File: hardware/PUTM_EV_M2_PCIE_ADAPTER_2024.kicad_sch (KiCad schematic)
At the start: 2 parts, among them J1 PCIE-064-02-X-D-RA, J2 M_2_EdgeConector

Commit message: high speed signals routing done
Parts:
- added C1, C3, C5: 100nF, Capacitor_SMD:C_0402_1005Metric, symbol Device:C_Small
- added C2, C4, C6, C7, C8, C9: 1uF, Capacitor_SMD:C_0603_1608Metric, symbol Device:C_Small
- added J3: PCB_WIRE, Connector_Wire:SolderWire-0.1sqmm_1x04_P3.6mm_D0.4mm_OD1mm_Relief, symbol Connector:Conn_01x04_Pin
- added R1: 0, Resistor_SMD:R_0402_1005Metric, symbol Device:R_Small
- J2: value M_2_EdgeConector -> M2_KEY_M; footprint M2-PCIe-adapter-footprints:M_2_EdgeConnector -> Snapeda:M.2-KEY-M
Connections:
- net GND: now reaches J2.1 (GND)
- net GND: now also J1.A04 (GND), J1.A12 (GND), J1.A15 (GND), J1.A18 (GND), J1.A20 (GND), J1.A23 (GND), J1.A24 (GND), J1.A27 (GND), J1.A28 (GND), J1.A31 (GND), J1.B04 (GND), J1.B07 (GND), J1.B13 (GND), J1.B16 (GND), J1.B18 (GND), J1.B21 (GND), J1.B22 (GND), J1.B25 (GND), J1.B26 (GND), J1.B29 (GND), J1.B32 (GND), J2.15 (GND), J2.21 (GND), J2.27 (GND), J2.3 (GND), J2.33 (GND), J2.39 (GND), J2.45 (GND), J2.51 (GND), J2.52 (CLKREQ#), J2.57 (GND), J2.71 (GND), J2.73 (GND), J2.75 (GND), J2.9 (GND), J2.MH, C1.2, C2.2, C3.2, C4.2, C5.2, C6.2, C7.2, C8.2, C9.2, J3.2 (Pin_2), J3.3 (Pin_3)
- net DO3-: now reaches J2.11 (PET3-)
- net DO3-: now also J1.B28 (DO3-)
- net +3.3V: now reaches J2.12 (+3.3V)
- net +3.3V: now also J1.A09 (+3.3V), J1.A10 (+3.3V), J1.B08 (+3.3V), J2.14 (+3.3V), J2.16 (+3.3V), J2.18 (+3.3V), J2.2 (+3.3V), J2.4 (+3.3V), J2.70 (+3.3V), J2.72 (+3.3V), J2.74 (+3.3V), C3.1, C4.1, C7.1, C8.1, C9.1, R1.1
- net DO3+: now reaches J2.13 (PET3+)
- net DO3+: now also J1.B27 (DO3+)
- net DI2-: now reaches J2.17 (PER2-)
- net DI2-: now also J1.A26 (DI2-)
- net DI2+: now reaches J2.19 (PER2+)
- net DI2+: now also J1.A25 (DI2+)
- net DO2-: now reaches J2.23 (PET2-)
- net DO2-: now also J1.B24 (DO2-)
- net DO2+: now reaches J2.25 (PET2+)
- net DO2+: now also J1.B23 (DO2+)
- net DI1-: now reaches J2.29 (PER1-)
- net DI1-: now also J1.A22 (DI1+)
- net DI1+: now reaches J2.31 (PER1+)
- net DI1+: now also J1.A21 (DI1+)
- net DO1-: now reaches J2.35 (PET1-)
- net DO1-: now also J1.B20 (DO1-)
- net DO1+: now reaches J2.37 (PET1+)
- net DO1+: now also J1.B19 (DO1+)
- net DI0-: now reaches J2.41 (SATA-B+/PER0-)
- net DI0-: now also J1.A17 (DI0-)
- net DI0+: now reaches J2.43 (SATA-B-/PER0+)
- net DI0+: now also J1.A16 (DI0+)
- net DO0-: now reaches J2.47 (SATA-A-/PET0-)
- net DO0-: now also J1.B15 (DO0-)
- net DO0+: now reaches J2.49 (SATA-A+/PET0+)
- net DO0+: now also J1.B14 (DO0+)
- net DI3-: now reaches J2.5 (PER3-)
- net DI3-: now also J1.A30 (DI3-)
- net PWRGD: now reaches J2.50 (PERST#)
- net PWRGD: now also J1.A11 (PWRGD)
- net REFCLK-: now reaches J2.53 (REFCLK-)
- net REFCLK-: now also J1.A14 (REFCLK-)
- net WAKE#: now reaches J2.54 (PEWAKE#)
- net WAKE#: now also J1.B11 (WAKE#)
- net REFCLK+: now reaches J2.55 (REFCLK+)
- net REFCLK+: now also J1.A13 (REFCLK+)
- net DI3+: now reaches J2.7 (PER3+)
- net DI3+: now also J1.A29 (DI3+)
- net +3.3AUX: now reaches J1.B10 (+3.3VAUX)
- net +3.3AUX: now also C5.1, C6.1, R1.2
- new net +12V: C1.1, C2.1, J1.A02 (+12V), J1.A03 (+12V), J1.B01 (+12V), J1.B02 (+12V), J1.B03 (+12V), J3.1 (Pin_1)
- new net +5V: J3.4 (Pin_4)
- no-connect marks 0 -> 17
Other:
- moved on the sheet: J1

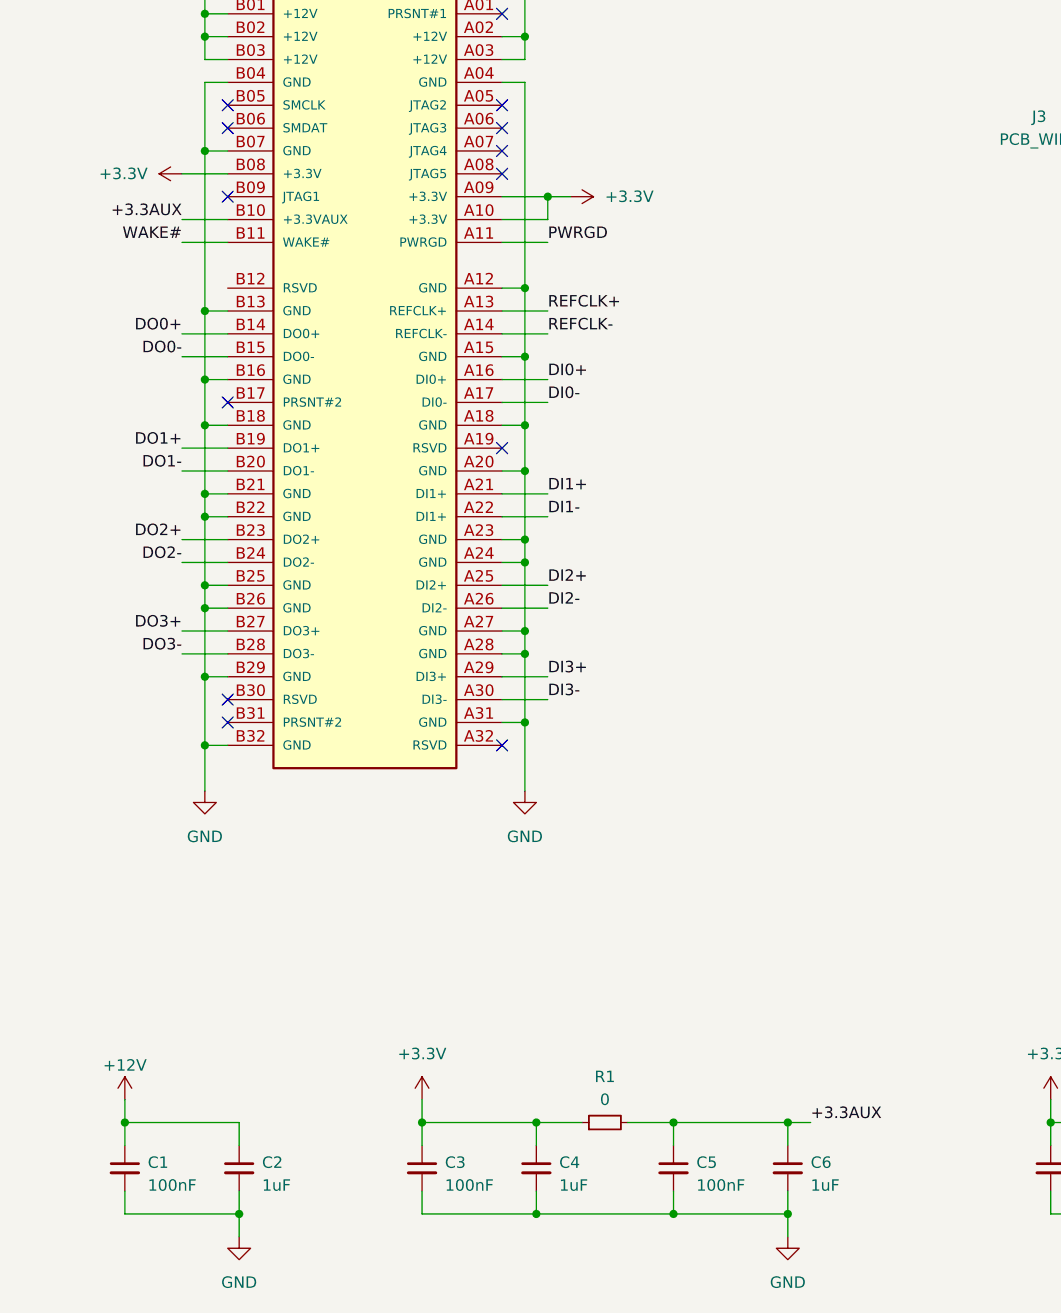
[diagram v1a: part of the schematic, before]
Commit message: deleted all tracks, needs a bigger board
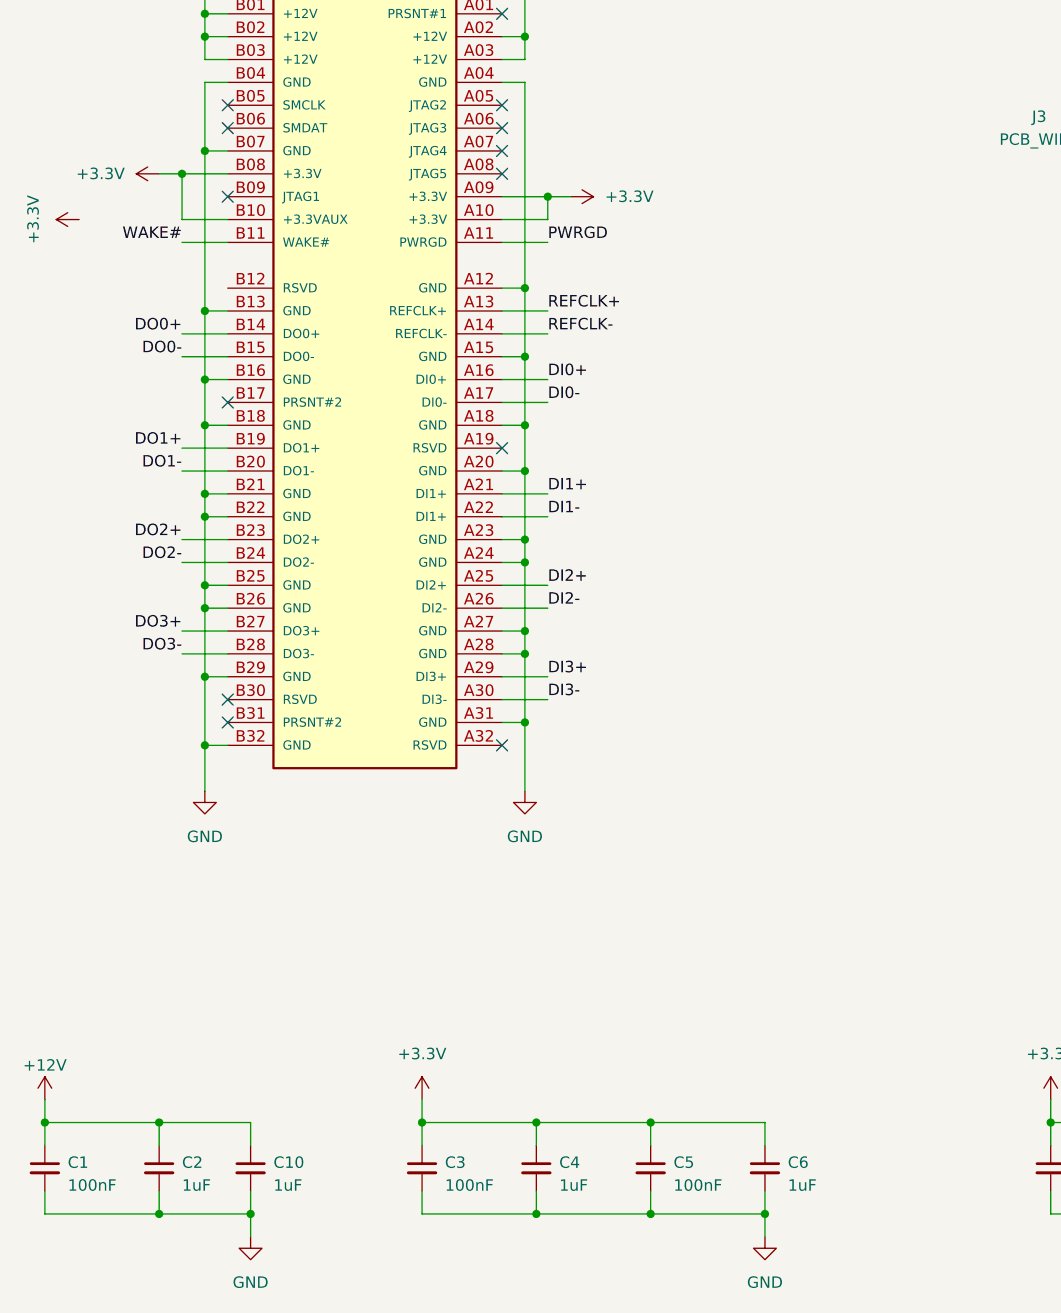
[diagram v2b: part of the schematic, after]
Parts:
- removed R1: 0, Resistor_SMD:R_0402_1005Metric, symbol Device:R_Small
- added C10: 1uF, Capacitor_SMD:C_0603_1608Metric, symbol Device:C_Small
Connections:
- net +3.3AUX is gone; now on net +3.3V: C5.1, C6.1, J1.B10 (+3.3VAUX)
- net +12V: now also C10.1
- net GND: now also C10.2
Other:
- moved on the sheet: C1, C2, C5, C6

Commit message: final design
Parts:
- J2: footprint Snapeda:M.2-KEY-M -> Snapeda:M.2-KEY-M-FAT
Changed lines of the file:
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@@
 			)
 		)
-		(property "Footprint" "Snapeda:M.2-KEY-M"
+		(property "Footprint" "Snapeda:M.2-KEY-M-FAT"
 			(at 198.12 80.01 0)
 			(effects
